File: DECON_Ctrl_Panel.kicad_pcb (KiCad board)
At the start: 2 copper layers, 174 x 106 mm, 275 parts, among them J1 Conn_01x02, J10 Conn_01x04, J11 Conn_01x06, J12 Conn_01x06, J13 Conn_01x04, J18 Conn_01x04, J2 GPIO, J3 Conn_01x06, J4 Conn_01x06, J5 FLASH, J6 Conn_01x06, J7 Conn_01x05, J8 Conn_01x06, J9 Conn_01x06, K1 G5NB, K10 G5NB, K11 G5NB, K12 G5NB, K13 G5NB, K14 G5NB, K15 G5NB, K16 G5NB, K17 G5NB, K2 G5NB, K3 G5NB, K4 G5NB, K5 G5NB, K6 G5NB, K7 G5NB, K8 G5NB, K9 G5NB, Q1 MMBT2222A, Q10 MMBT2222A, Q11 MMBT2222A, Q12 MMBT2222A, Q13 MMBT2222A, Q14 MMBT2222A, Q15 MMBT2222A, Q16 MMBT2222A, Q2 MMBT2222A, Q3 MMBT2222A, Q4 MMBT2222A, Q5 MMBT2222A, Q6 MMBT2222A, Q7 MMBT2222A, Q8 MMBT2222A, Q9 MMBT2222A, SW1 SW_Push, SW2 SW_Push, U1 URB2405YMD-10WR3, U10 LTV-817S, U11 LTV-817S, U12 LTV-817S, U13 LTV-817S, U14 LTV-817S, U15 LTV-817S, U16 LTV-817S, U17 LTV-817S, U18 LTV-817S, U19 LTV-817S, U2 AZ1117-3.3, U20 74HC138, U21 LTV-817S, U22 LTV-817S, U23 LTV-817S, U24 LTV-817S, U25 LTV-817S, U26 LTV-817S, U27 LTV-817S, U28 LTV-817S, U29 LTV-817S, U3 STM32F401R_B-C_Tx, U30 LTV-817S, U31 LTV-817S, U32 LTV-817S, U33 LTV-817S, U34 LTV-817S, U35 LTV-817S, U36 LTV-817S, U4 LTV-817S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

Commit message: modified:   DECON_Ctrl_Panel.kicad_prl
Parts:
- moved C18 73.3 mm to (166.4, 87.9), turned to 90 degrees
- moved C17 65.6 mm to (174.6, 96.3), turned to 90 degrees
- moved C16 63.4 mm to (176.3, 89.7), turned to 0 degrees
- moved C15 59.1 mm to (181.2, 85.1), turned to -90 degrees
- moved C20 55.9 mm to (179.6, 102.2), turned to 90 degrees
- moved C21 52.8 mm to (189.2, 104.0), turned to -90 degrees
- moved C12 46.3 mm to (193.8, 90.4)
- moved C19 38.8 mm to (191.3, 104.0), turned to 90 degrees
- moved U3 2.71 mm to (184.9, 93.9)
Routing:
- net MCU_SS_0: track 2.95 -> 79.0 mm
- net GND_MCU: track 56.0 -> 0.00 mm
- net MCU_EXTI: track 39.9 -> 61.7 mm
- net MCU_RL4: track 15.6 -> 29.4 mm
- net MCU_RL2: track 30.5 -> 43.6 mm
- net MCU_RL3: track 23.4 -> 36.3 mm
- net MCU_SS_1: track 58.6 -> 70.2 mm
- net MCU_RL1: track 39.0 -> 49.8 mm
- net MCU_RL0: track 47.6 -> 57.8 mm
- net MCU_RL6: track 6.74 -> 15.5 mm, vias 1 -> 0
- net MCU_RL5: track 13.3 -> 21.7 mm, vias 1 -> 0
- net MCU_RL12: track 53.9 -> 47.3 mm
- net MCU_RL8: track 22.7 -> 29.1 mm
- net MCU_RL7: track 15.4 -> 21.8 mm
- net MCU_RL9: track 30.4 -> 36.4 mm
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
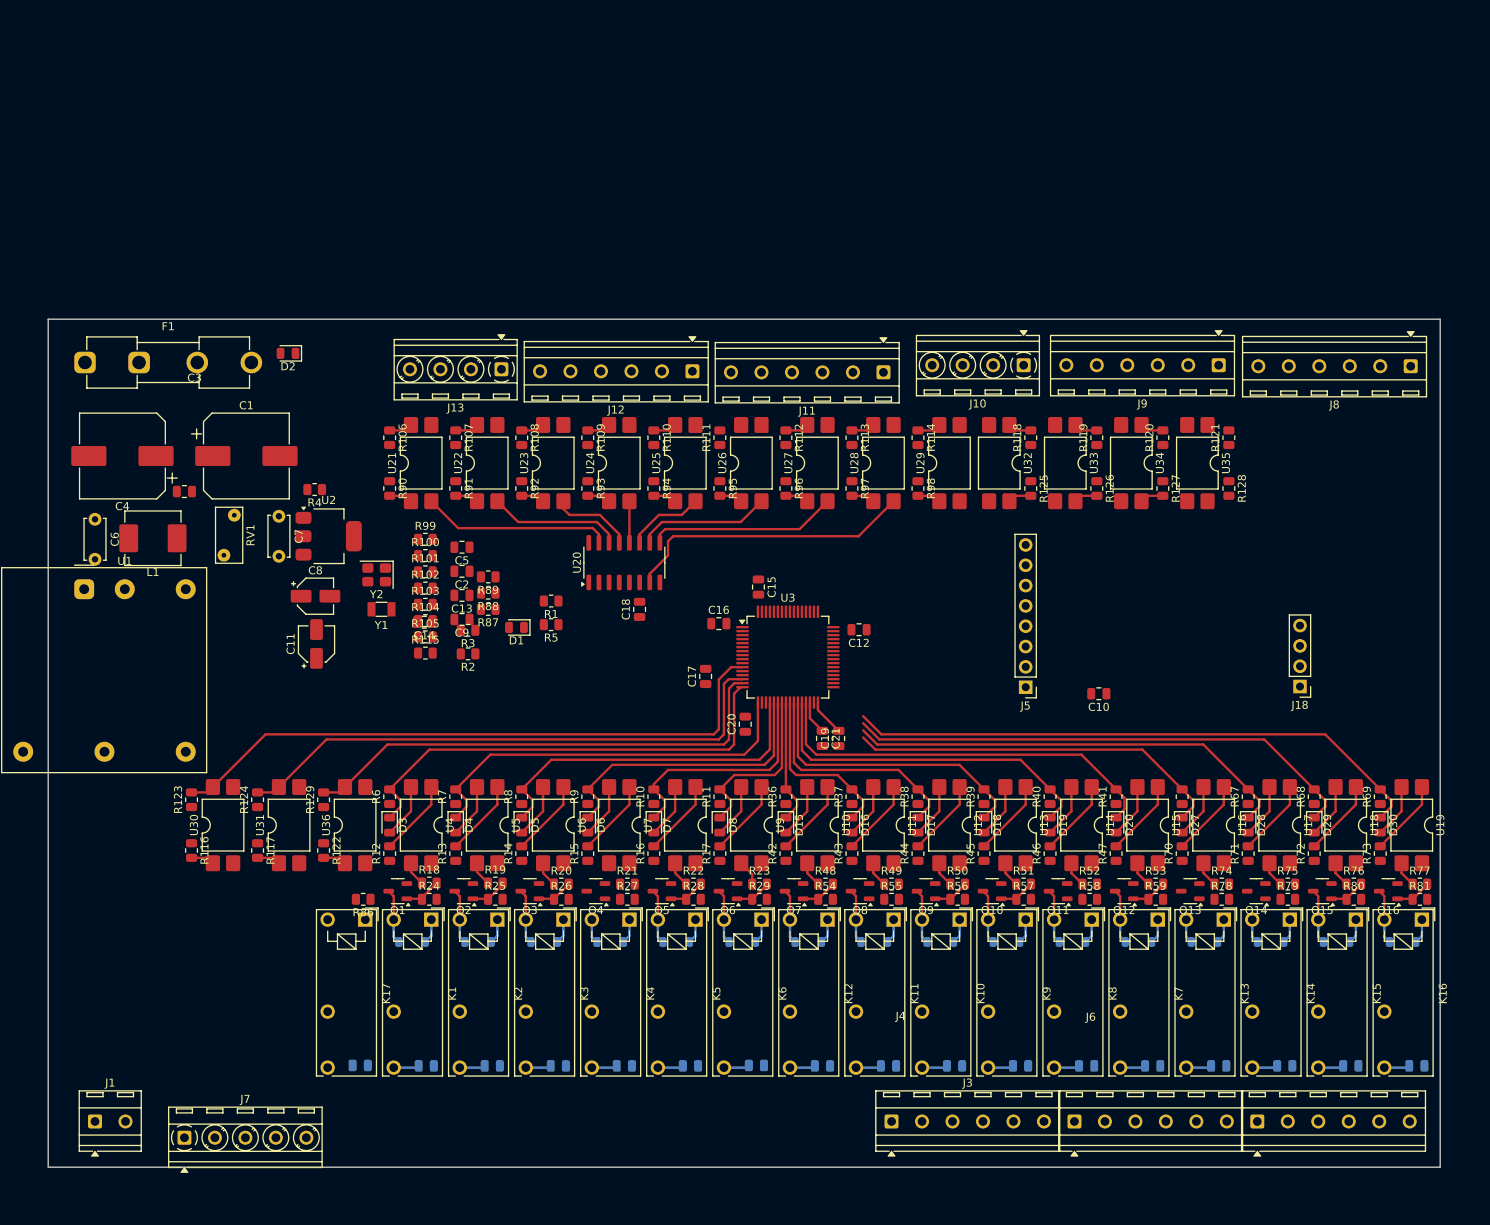
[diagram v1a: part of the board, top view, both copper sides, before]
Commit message: modified:   DECON_Ctrl_Panel.kicad_pcb 	modified:   DECON_Ctrl_Panel.kicad_prl 	modified:   decon_mcu.kicad_sch
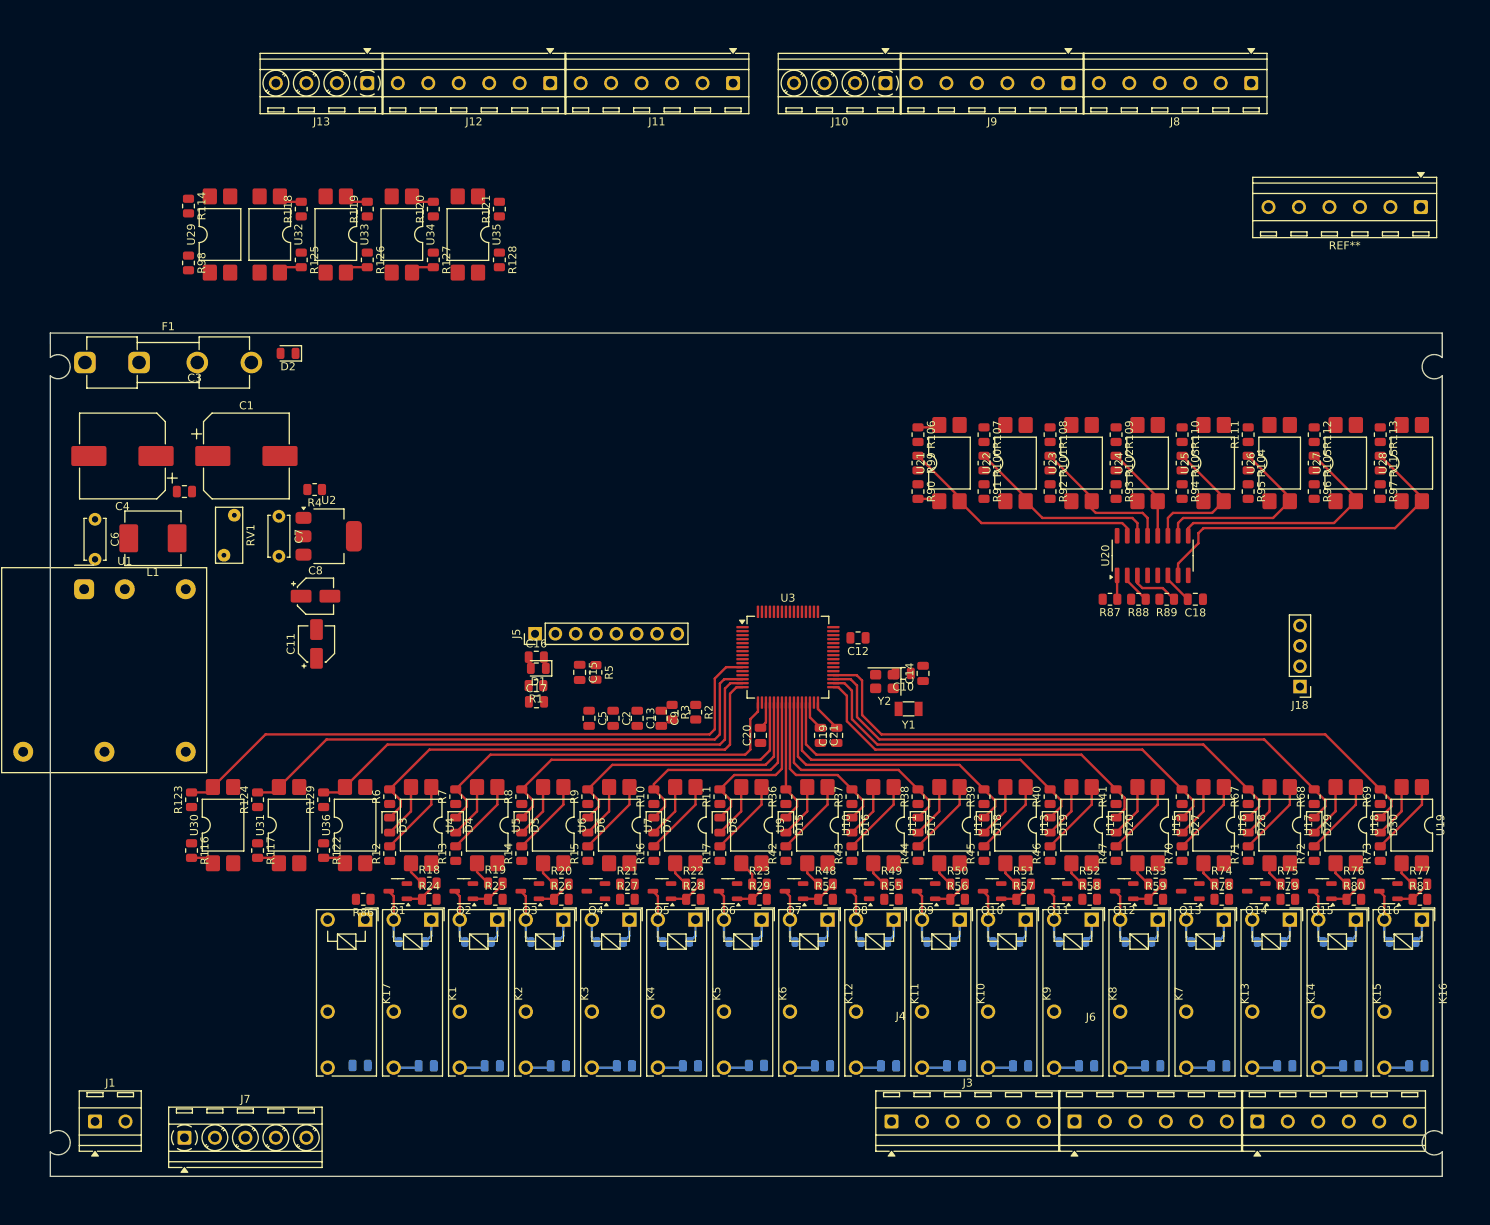
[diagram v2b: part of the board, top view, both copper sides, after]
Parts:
- added REF**: TerminalBlock_MetzConnect_Type086_RT03406HBLC_1x06_P3.81mm_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, TerminalBlock_MetzConnect:TerminalBlock_MetzConnect_Type086_RT03406HBLC_1x06_P3.81mm_Horizontal, F.Cu at (264.0, 37.6)
- moved R115 121.7 mm to (259.0, 69.6), turned to -90 degrees
- moved R105 113.2 mm to (250.7, 69.6), turned to -90 degrees
- moved R104 104.7 mm to (242.4, 69.6), turned to -90 degrees
- moved R103 96.2 mm to (234.2, 69.6), turned to -90 degrees
- moved R114 95.7 mm to (110.0, 37.5)
- moved R120 95.6 mm to (140.6, 37.8)
- moved R121 95.6 mm to (148.8, 37.8)
- moved R127 95.6 mm to (140.6, 44.2)
- moved R128 95.6 mm to (148.8, 44.2)
- moved U32 95.6 mm to (120.1, 41.0)
- moved U33 95.6 mm to (128.4, 41.0)
- moved U34 95.6 mm to (136.7, 41.0)
- moved R118 95.6 mm to (124.1, 37.8)
- moved R125 95.6 mm to (124.1, 44.2)
- moved U29 95.6 mm to (113.9, 41.0)
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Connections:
- J10 pad 1: LED_4 -> BUTTON_0
- J10 pad 2: LED_5 -> BUTTON_EN
- J10 pad 3: LED_6 -> GND_VBAT
- J10 pad 4: EXT_OUTPUT -> VBAT
- J11 pad 1: VBAT -> EXT_OUTPUT
- J11 pad 2: GND_VBAT -> LED_6
- J11 pad 3: BUTTON_EN -> LED_5
- J11 pad 4: BUTTON_0 -> LED_4
- J11 pad 5: BUTTON_1 -> LED_3
- J11 pad 6: BUTTON_2 -> LED_2
- J12 pad 1: BUTTON_3 -> LED_1
- J12 pad 2: LED_POWER -> LED_0
- J12 pad 3: LED_0 -> LED_POWER
- J12 pad 4: LED_1 -> BUTTON_3
- J12 pad 5: LED_2 -> BUTTON_2
- J12 pad 6: LED_3 -> BUTTON_1
- J13 pad 1: LED_4 -> BUTTON_0
- J13 pad 2: LED_5 -> BUTTON_EN
- J13 pad 3: LED_6 -> GND_VBAT
- J13 pad 4: EXT_OUTPUT -> VBAT
- J8 pad 1: VBAT -> EXT_OUTPUT
- J8 pad 2: GND_VBAT -> LED_6
- J8 pad 3: BUTTON_EN -> LED_5
- J8 pad 4: BUTTON_0 -> LED_4
- J8 pad 5: BUTTON_1 -> LED_3
- J8 pad 6: BUTTON_2 -> LED_2
- J9 pad 1: BUTTON_3 -> LED_1
- J9 pad 2: LED_POWER -> LED_0
- J9 pad 3: LED_0 -> LED_POWER
- J9 pad 4: LED_1 -> BUTTON_3
- J9 pad 5: LED_2 -> BUTTON_2
- J9 pad 6: LED_3 -> BUTTON_1
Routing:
- net MCU_RL15: track 73.1 -> 81.5 mm
- net MCU_RL14: track 64.5 -> 72.8 mm
- net 74138_Y2: track 10.2 -> 18.5 mm
- net MCU_RL13: track 55.9 -> 64.1 mm
- net MCU_RL12: track 47.3 -> 55.4 mm
- net 74138_Y4: track 9.65 -> 17.7 mm
- net 74138_Y5: track 16.8 -> 24.5 mm
- net 74138_Y1: track 16.8 -> 24.5 mm
- net 74138_Y0: track 23.7 -> 31.1 mm
- net 74138_Y7: track 36.4 -> 43.8 mm
- net 74138_Y6: track 23.7 -> 31.1 mm
- net 3.3V: track 4.61 -> 11.6 mm
- net 74138_Y3: track 5.20 -> 12.2 mm
- net MCU_A2: track 0.00 -> 6.38 mm
- net MCU_A1: track 0.00 -> 3.94 mm
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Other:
- board size 174 x 106 mm -> 174 x 105.4 mm

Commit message: modified:   DECON_Ctrl_Panel.kicad_pcb 	modified:   DECON_Ctrl_Panel.kicad_prl 	modified:   DECON_Ctrl_Panel.kicad_pro
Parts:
- removed J1: Conn_01x02, TerminalBlock_MetzConnect:TerminalBlock_MetzConnect_Type086_RT03402HBLC_1x02_P3.81mm_Horizontal
- added REF**: TerminalBlock_Phoenix_MKDS-1-13-3.81_1x13_P3.81mm_Horizontal, TerminalBlock_Phoenix:TerminalBlock_Phoenix_MKDS-1-13-3.81_1x13_P3.81mm_Horizontal, F.Cu at (158.5, 167.1)
- moved R114 90.0 mm to (192.9, 72.5)
- moved R98 90.0 mm to (192.9, 79.6)
- moved U29 90.0 mm to (196.8, 76.1)
- moved C8 58.5 mm to (80.6, 49.0)
- moved D2 58.5 mm to (77.2, 18.7)
- moved F1 58.5 mm to (51.8, 19.8)
- moved C1 58.5 mm to (72.0, 31.5)
- moved C7 58.5 mm to (76.1, 39.1)
- moved R4 58.5 mm to (80.5, 35.7)
- moved RV1 58.5 mm to (69.2, 43.9)
- moved C11 58.5 mm to (80.8, 55.0)
- moved U2 58.5 mm to (82.3, 41.6)
- moved U32 56.0 mm to (163.8, 76.1)
- moved U33 56.0 mm to (172.1, 76.1)
- moved U34 56.0 mm to (180.3, 76.1)
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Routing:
- net VBAT: track 0.00 -> 101.7 mm
- net EXT_OUTPUT: track 0.00 -> 94.9 mm, vias 0 -> 1
- net LED_6: track 0.00 -> 88.6 mm, vias 0 -> 1
- net LED_5: track 0.00 -> 83.9 mm, vias 0 -> 1
- net LED_4: track 0.00 -> 81.3 mm, vias 0 -> 1
- net LED_3: track 0.00 -> 78.7 mm, vias 0 -> 1
- net LED_2: track 0.00 -> 76.6 mm, vias 0 -> 1
- net LED_1: track 0.00 -> 76.6 mm, vias 0 -> 1
- net BUTTON_0: track 0.00 -> 76.6 mm, vias 0 -> 1
- net BUTTON_1: track 0.00 -> 76.6 mm, vias 0 -> 1
- net LED_POWER: track 0.00 -> 76.6 mm, vias 0 -> 1
- net LED_0: track 0.00 -> 76.6 mm, vias 0 -> 1
- net BUTTON_3: track 0.00 -> 76.6 mm, vias 0 -> 1
- net BUTTON_2: track 0.00 -> 76.6 mm, vias 0 -> 1
- net BUTTON_EN: track 0.00 -> 67.8 mm
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
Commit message: modified:   DECON_Ctrl_Panel.kicad_pcb 	modified:   DECON_Ctrl_Panel.kicad_prl 	modified:   decon_mcu.kicad_sch
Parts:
- removed REF**: TerminalBlock_Phoenix_MKDS-1-13-3.81_1x13_P3.81mm_Horizontal, TerminalBlock_Phoenix:TerminalBlock_Phoenix_MKDS-1-13-3.81_1x13_P3.81mm_Horizontal
- removed REF**: TerminalBlock_MetzConnect_Type086_RT03406HBLC_1x06_P3.81mm_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, TerminalBlock_MetzConnect:TerminalBlock_MetzConnect_Type086_RT03406HBLC_1x06_P3.81mm_Horizontal
- added J1: Conn_01x02, TerminalBlock_MetzConnect:TerminalBlock_MetzConnect_Type086_RT03402HBLC_1x02_P3.81mm_Horizontal, F.Cu at (130.4, 57.5)
- J2: value GPIO -> Conn_01x02; footprint Connector_PinHeader_2.54mm:PinHeader_1x12_P2.54mm_Vertical -> Connector_PinHeader_2.54mm:PinHeader_1x02_P2.54mm_Vertical
- moved SW2 122.6 mm to (164.6, 99.7)
- moved SW1 88.3 mm to (207.8, 99.6)
- moved C1 74.9 mm to (136.9, 69.0)
- moved U1 69.0 mm to (128.2, 80.7)
- moved F1 60.8 mm to (99.6, 57.5)
- moved C4 57.9 mm to (120.4, 69.0)
- moved R1 52.3 mm to (204.3, 103.8), turned to -90 degrees
- moved D1 49.6 mm to (201.4, 103.5), turned to -90 degrees
- moved C2 46.6 mm to (209.6, 104.0)
- moved J18 46.2 mm to (212.5, 85.9), turned to 90 degrees
- moved J5 38.2 mm to (191.5, 85.9)
- moved R2 33.5 mm to (206.8, 103.9), turned to 90 degrees
- moved C16 24.7 mm to (178.1, 90.8)
- moved C18 22.7 mm to (215.6, 103.4), turned to 90 degrees
- moved C17 20.0 mm to (172.7, 104.8)
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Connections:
- C2 pad 1: MCU_BTN_4 -> PA8
- J2 pad 1: PA15 -> PA8
- J2 pad 2: PC10 -> PC9
- R2 pad 2: MCU_BTN_4 -> PA8
- SW1 pad 1: MCU_BTN_4 -> PA8
- U3 pad 10: MCU_A0 -> PC2
- U3 pad 3: PC14 -> OSC32_IN
- U3 pad 37: MCU_BTN_0 -> MCU_A2
- U3 pad 38: MCU_BTN_1 -> MCU_A1
- U3 pad 39: MCU_BTN_2 -> MCU_A0
- U3 pad 4: PC15 -> OSC32_OUT
- U3 pad 40: MCU_BTN_3 -> PC9
- U3 pad 41: MCU_BTN_4 -> PA8
- U3 pad 44: unconnected-(U3-PA11-Pad44) -> MCD_D-
- U3 pad 45: unconnected-(U3-PA12-Pad45) -> MCD_D+
- U3 pad 46: unconnected-(U3-PA13-Pad46) -> PA13
- U3 pad 49: unconnected-(U3-PA14-Pad49) -> PA14
- U3 pad 5: PH0 -> OSC_IN
- U3 pad 57: PB5 -> MCU_BTN_4
- U3 pad 58: PB6 -> MCU_BTN_3
- U3 pad 59: PB7 -> MCU_BTN_2
- U3 pad 6: PH1 -> OSC_OUT
- U3 pad 61: PB8 -> MCU_BTN_1
- U3 pad 62: PB9 -> MCU_BTN_0
- U3 pad 8: MCU_A2 -> PC0
- U3 pad 9: MCU_A1 -> PC1
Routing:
- net V_VALVE: track 49.8 -> 355.2 mm
- net 74138_Y7: track 43.8 -> 93.0 mm
- net 74138_Y6: track 31.1 -> 74.1 mm
- net 74138_Y5: track 24.5 -> 65.3 mm
- net 74138_Y3: track 12.2 -> 47.8 mm
- net 74138_Y4: track 26.3 -> 56.6 mm
- net PC12: track 0.00 -> 27.9 mm
- net PD2: track 0.00 -> 27.3 mm
- net PB3: track 0.00 -> 25.6 mm
- net PC11: track 0.00 -> 21.4 mm
- net 74138_Y0: track 31.1 -> 10.3 mm
- net PB4: track 0.00 -> 20.6 mm
- net 74138_Y2: track 18.5 -> 39.0 mm
- net MCU_BTN_4: track 0.00 -> 19.4 mm
- net MCU_BTN_3: track 6.40 -> 24.1 mm
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
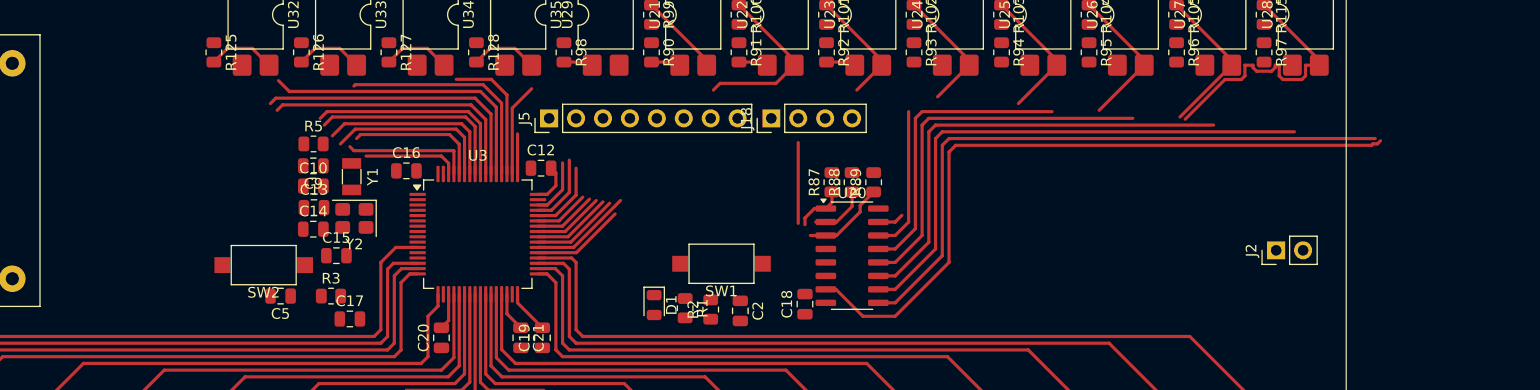
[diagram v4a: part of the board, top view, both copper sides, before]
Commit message: modified:   DECON_Ctrl_Panel.kicad_pcb 	modified:   DECON_Ctrl_Panel.kicad_prl 	modified:   button_sensor.kicad_sch 	modified:   decon_mcu.kicad_sch
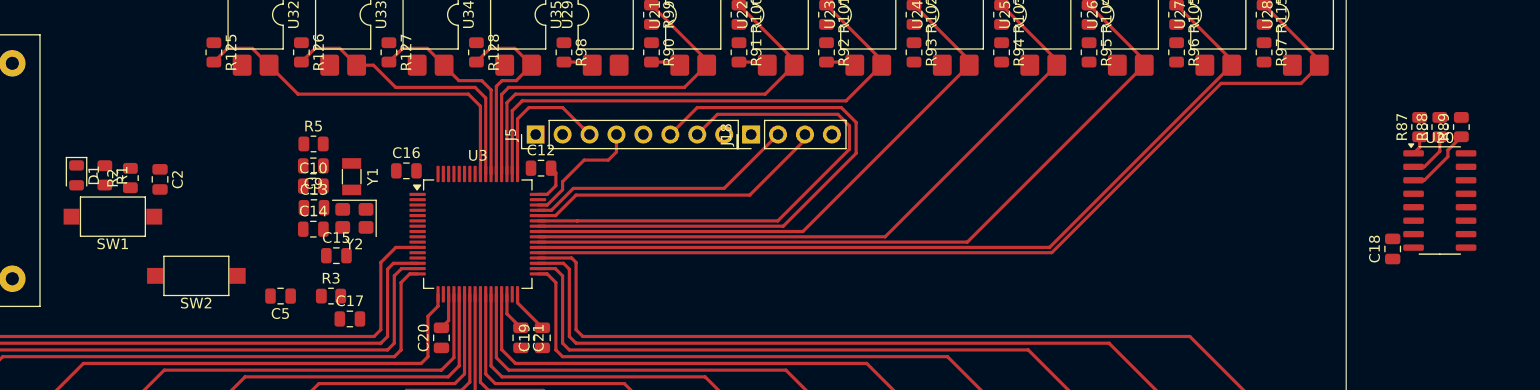
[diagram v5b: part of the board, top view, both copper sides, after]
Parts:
- removed J2: Conn_01x02, Connector_PinHeader_2.54mm:PinHeader_1x02_P2.54mm_Vertical
- moved SW1 57.6 mm to (150.4, 95.1)
- moved R1 56.2 mm to (149.6, 91.2)
- moved C2 56.1 mm to (154.8, 91.6)
- moved R2 56.1 mm to (152.0, 91.5)
- moved D1 55.8 mm to (146.9, 91.2)
- moved C18 55.7 mm to (271.1, 98.2)
- moved R88 55.7 mm to (275.5, 86.7)
- moved R89 55.7 mm to (277.6, 86.7)
- moved U20 55.7 mm to (275.5, 93.6)
- moved R87 55.7 mm to (273.6, 86.7)
- moved SW2 6.43 mm to (158.2, 100.7)
- moved J18 2.44 mm to (210.6, 87.4)
- moved J5 1.98 mm to (190.2, 87.4)
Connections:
- net MCU_BTN_4 renamed PB5
- C2 pad 1: PA8 -> 74138_Y3
- R2 pad 2: PA8 -> 74138_Y3
- R87 pad 1: MCU_A0 -> Net-(U20-A0)
- R87 pad 2: 3.3V -> Net-(U20-VCC)
- R88 pad 1: MCU_A1 -> Net-(U20-A1)
- R88 pad 2: 3.3V -> Net-(U20-VCC)
- R89 pad 1: MCU_A2 -> Net-(U20-A2)
- R89 pad 2: 3.3V -> Net-(U20-VCC)
- SW1 pad 1: PA8 -> 74138_Y3
- U20 pad 1: MCU_A0 -> Net-(U20-A0)
- U20 pad 10: 74138_Y5 -> unconnected-(U20-~{Y5}-Pad10)
- U20 pad 11: 74138_Y4 -> unconnected-(U20-~{Y4}-Pad11)
- U20 pad 12: 74138_Y3 -> unconnected-(U20-~{Y3}-Pad12)
- U20 pad 13: 74138_Y2 -> unconnected-(U20-~{Y2}-Pad13)
- U20 pad 14: 74138_Y1 -> unconnected-(U20-~{Y1}-Pad14)
- U20 pad 15: 74138_Y0 -> unconnected-(U20-~{Y0}-Pad15)
- U20 pad 16: 3.3V -> Net-(U20-VCC)
- U20 pad 2: MCU_A1 -> Net-(U20-A1)
- U20 pad 3: MCU_A2 -> Net-(U20-A2)
- U20 pad 4: GND_MCU -> Net-(U20-~{E0})
- U20 pad 5: GND_MCU -> Net-(U20-~{E0})
- U20 pad 6: 3.3V -> unconnected-(U20-E2-Pad6)
- U20 pad 7: 74138_Y7 -> unconnected-(U20-~{Y7}-Pad7)
- U20 pad 8: GND_MCU -> unconnected-(U20-GND-Pad8)
- U20 pad 9: 74138_Y6 -> unconnected-(U20-~{Y6}-Pad9)
- U3 pad 37: MCU_A2 -> 74138_Y7
- U3 pad 38: MCU_A1 -> 74138_Y6
- U3 pad 39: MCU_A0 -> 74138_Y5
- U3 pad 40: PC9 -> 74138_Y4
- U3 pad 41: PA8 -> 74138_Y3
- U3 pad 50: PA15 -> 74138_Y2
- U3 pad 51: PC10 -> 74138_Y1
- U3 pad 52: PC11 -> 74138_Y0
- U3 pad 53: PC12 -> MCU_BTN_3
- U3 pad 54: PD2 -> MCU_BTN_2
- U3 pad 55: PB3 -> MCU_BTN_1
- U3 pad 56: PB4 -> MCU_BTN_0
- U3 pad 58: MCU_BTN_3 -> PB6
- U3 pad 59: MCU_BTN_2 -> PB7
- U3 pad 61: MCU_BTN_1 -> PB8
- U3 pad 62: MCU_BTN_0 -> PB9
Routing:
- net MCU_TX1: track 5.92 -> 54.9 mm
- net MCU_RX1: track 5.16 -> 50.0 mm
- net PC12: track 27.9 -> 0.00 mm
- net PD2: track 27.3 -> 0.00 mm
- net PB3: track 25.6 -> 0.00 mm
- net 74138_Y0: track 10.3 -> 35.8 mm
- net MCD_D-: track 6.94 -> 28.7 mm
- net PC11: track 21.4 -> 0.00 mm
- net PB4: track 20.6 -> 0.00 mm
- net PB5: track 19.4 -> 0.00 mm
- net MCD_D+: track 6.71 -> 25.6 mm
- net MCU_BTN_0: track 15.5 -> 34.3 mm
- net MCU_A2: track 16.8 -> 0.00 mm
- net PC9: track 15.1 -> 0.00 mm
- net MCU_A1: track 15.0 -> 0.00 mm
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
